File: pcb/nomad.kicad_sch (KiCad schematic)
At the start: 0 parts

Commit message: Fixing pcb project's .gitignore & initializing Kicad project
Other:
- title: (none) -> Nomad
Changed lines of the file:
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@@
 	(generator_version "10.0")
 	(paper "A4")
+	(title_block
+		(title "Nomad")
+		(rev "[In dev]")
+		(comment 1 "By @0Zane")
+		(comment 2 "Built for @Hackclub")
+	)
 	(sheet_instances
 		(path "/"

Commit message: Placing MCP9808 symbol
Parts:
- added R1, R2: 4.7k, symbol Device:R
- added U1: MCP9808_MSOP, Package_SO:MSOP-8_3x3mm_P0.65mm, symbol Sensor_Temperature:MCP9808_MSOP
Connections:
- new net: R1.2, U1.1 (SDA)
- new net: R2.2, U1.2 (SCL)
- new net +3V3: R1.1, R2.1, U1.8 (V_{DD})
- new net GND: U1.4 (GND)
- no-connect marks 0 -> 1

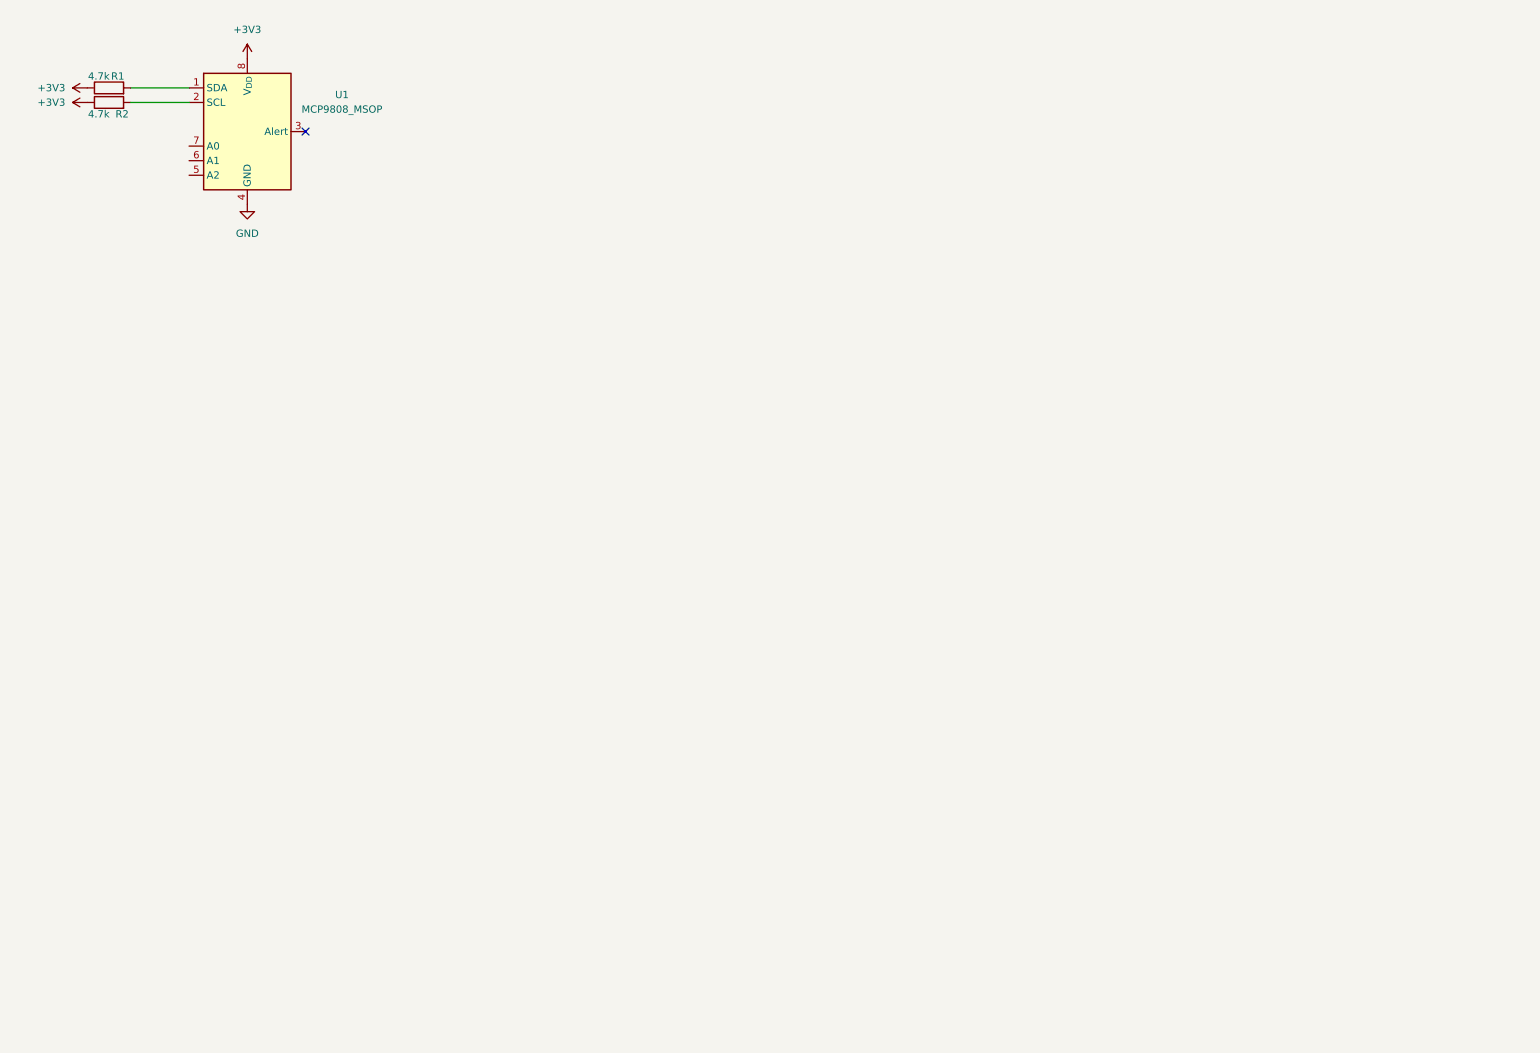
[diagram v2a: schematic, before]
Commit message: Wiring USB-C, MCP9808, PCF8574T
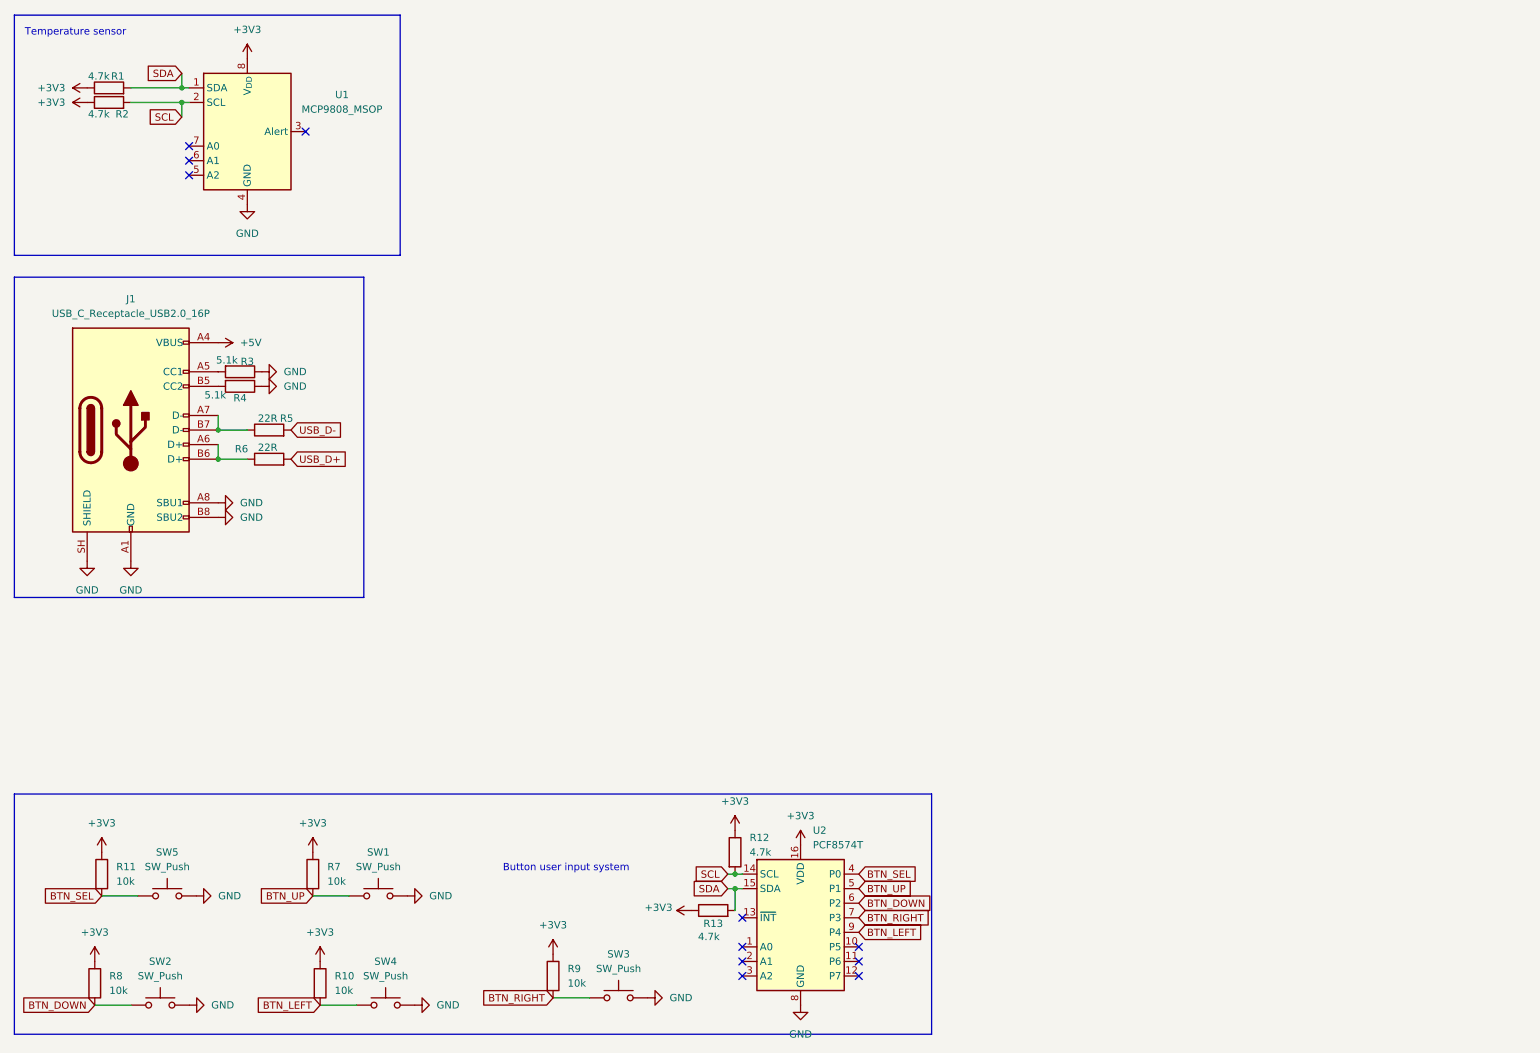
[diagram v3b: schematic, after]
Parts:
- added J1: USB_C_Receptacle_USB2.0_16P, symbol Connector:USB_C_Receptacle_USB2.0_16P
- added R10, R11, R7, R8, R9: 10k, symbol Device:R
- added R12, R13: 4.7k, symbol Device:R
- added R3, R4: 5.1k, symbol Device:R
- added R5, R6: 22R, symbol Device:R
- added SW1, SW2, SW3, SW4, SW5: SW_Push, symbol Switch:SW_Push
- added U2: PCF8574T, Package_SO:SOIC-16W_7.5x10.3mm_P1.27mm, symbol Interface_Expansion:PCF8574T
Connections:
- net +3V3: now also R10.1, R11.1, R12.1, R13.1, R7.1, R8.1, R9.1, U2.16 (VDD)
- net GND: now also J1.A1 (GND), J1.A12 (GND), J1.A8 (SBU1), J1.B1 (GND), J1.B12 (GND), J1.B8 (SBU2), J1.SH (SHIELD), R3.1, R4.1, SW1.2, SW2.2, SW3.2, SW4.2, SW5.2, U2.8 (GND)
- net SDA: now reaches R1.2, U1.1 (SDA)
- net SDA: now also R13.2, U2.15 (SDA)
- net SCL: now reaches R2.2, U1.2 (SCL)
- net SCL: now also R12.2, U2.14 (SCL)
- new net: J1.B5 (CC2), R4.2
- new net: J1.A6 (D+), J1.B6 (D+), R6.1
- new net: J1.A7 (D-), J1.B7 (D-), R5.1
- new net: J1.A5 (CC1), R3.2
- new net +5V: J1.A4 (VBUS), J1.A9 (VBUS), J1.B4 (VBUS), J1.B9 (VBUS)
- new net BTN_DOWN: R8.2, SW2.1, U2.6 (P2)
- new net BTN_LEFT: R10.2, SW4.1, U2.9 (P4)
- new net BTN_RIGHT: R9.2, SW3.1, U2.7 (P3)
- new net BTN_SEL: R11.2, SW5.1, U2.4 (P0)
- new net BTN_UP: R7.2, SW1.1, U2.5 (P1)
- new net USB_D+: R6.2
- new net USB_D-: R5.2
- no-connect marks 1 -> 11
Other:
- note added: "Button user input system"
- note added: "Temperature sensor"

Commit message: Replacing temperature sensor schematic + adding INT pin on PCF8574
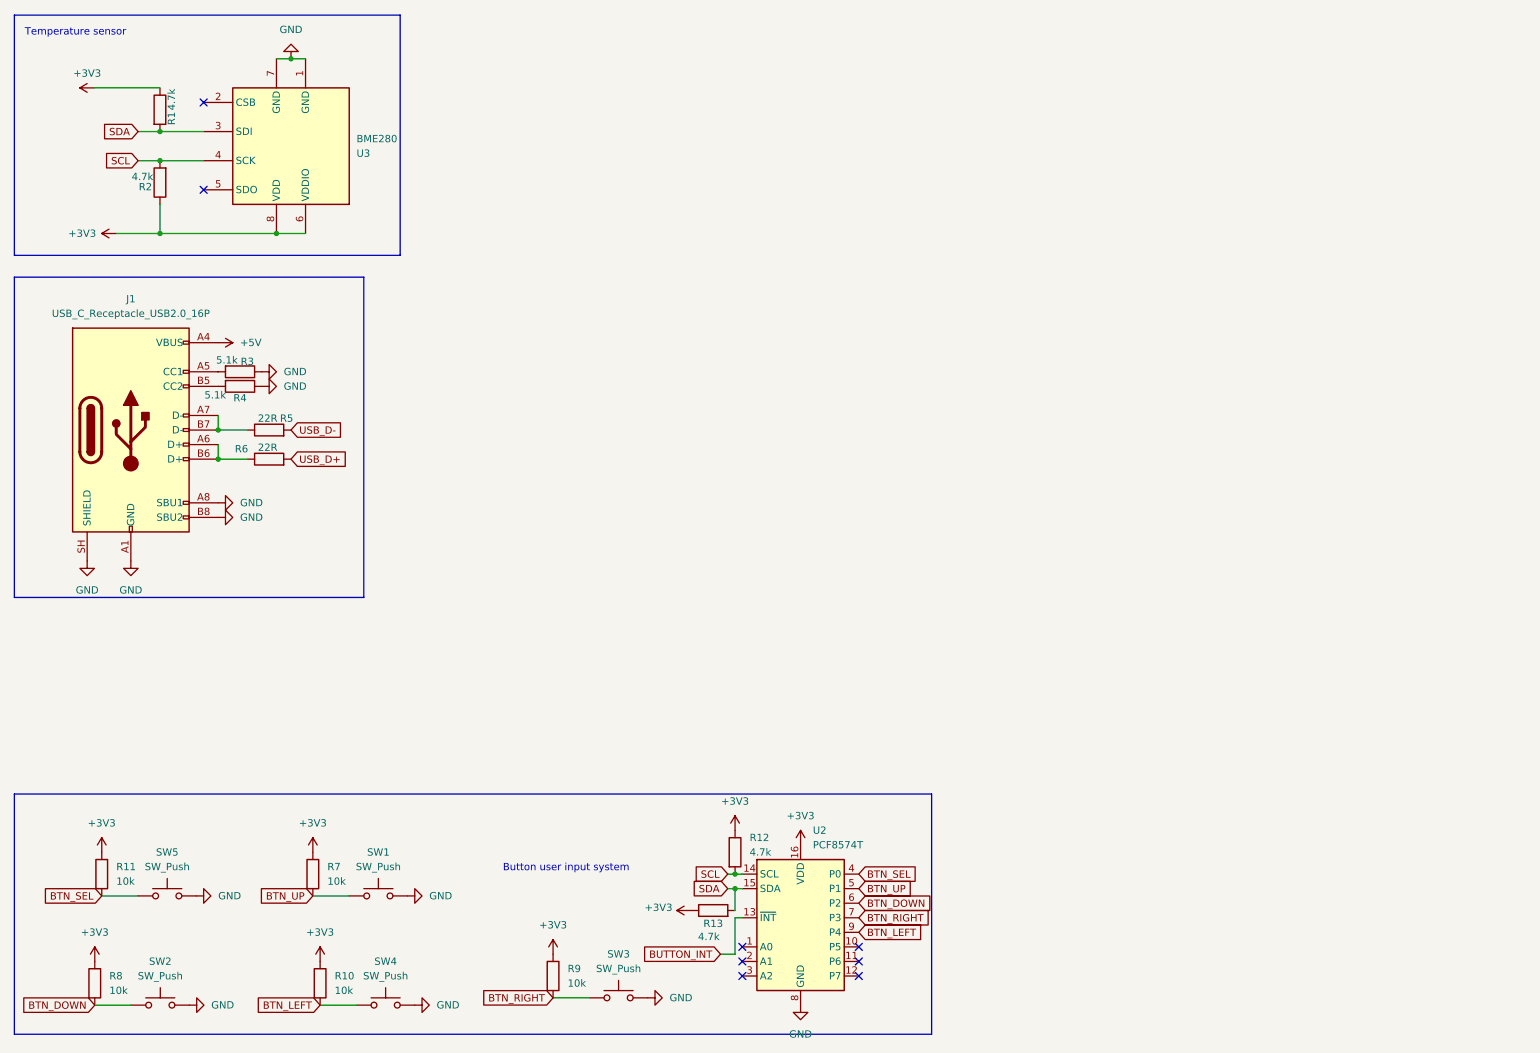
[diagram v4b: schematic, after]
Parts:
- removed U1: MCP9808_MSOP, Package_SO:MSOP-8_3x3mm_P0.65mm, symbol Sensor_Temperature:MCP9808_MSOP
- added U3: BME280, Package_LGA:Bosch_LGA-8_2.5x2.5mm_P0.65mm_ClockwisePinNumbering, symbol Sensor:BME280
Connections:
- net +3V3: now also U3.6 (VDDIO), U3.8 (VDD)
- net GND: now also U3.1 (GND), U3.7 (GND)
- net SCL: now also U3.4 (SCK)
- net SDA: now also U3.3 (SDI)
- net BUTTON_INT: now reaches U2.13 (~{INT})
- no-connect marks 11 -> 8
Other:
- moved on the sheet: R1, R2

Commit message: Adding BOOT & RESET buttons + ESP32 symbol
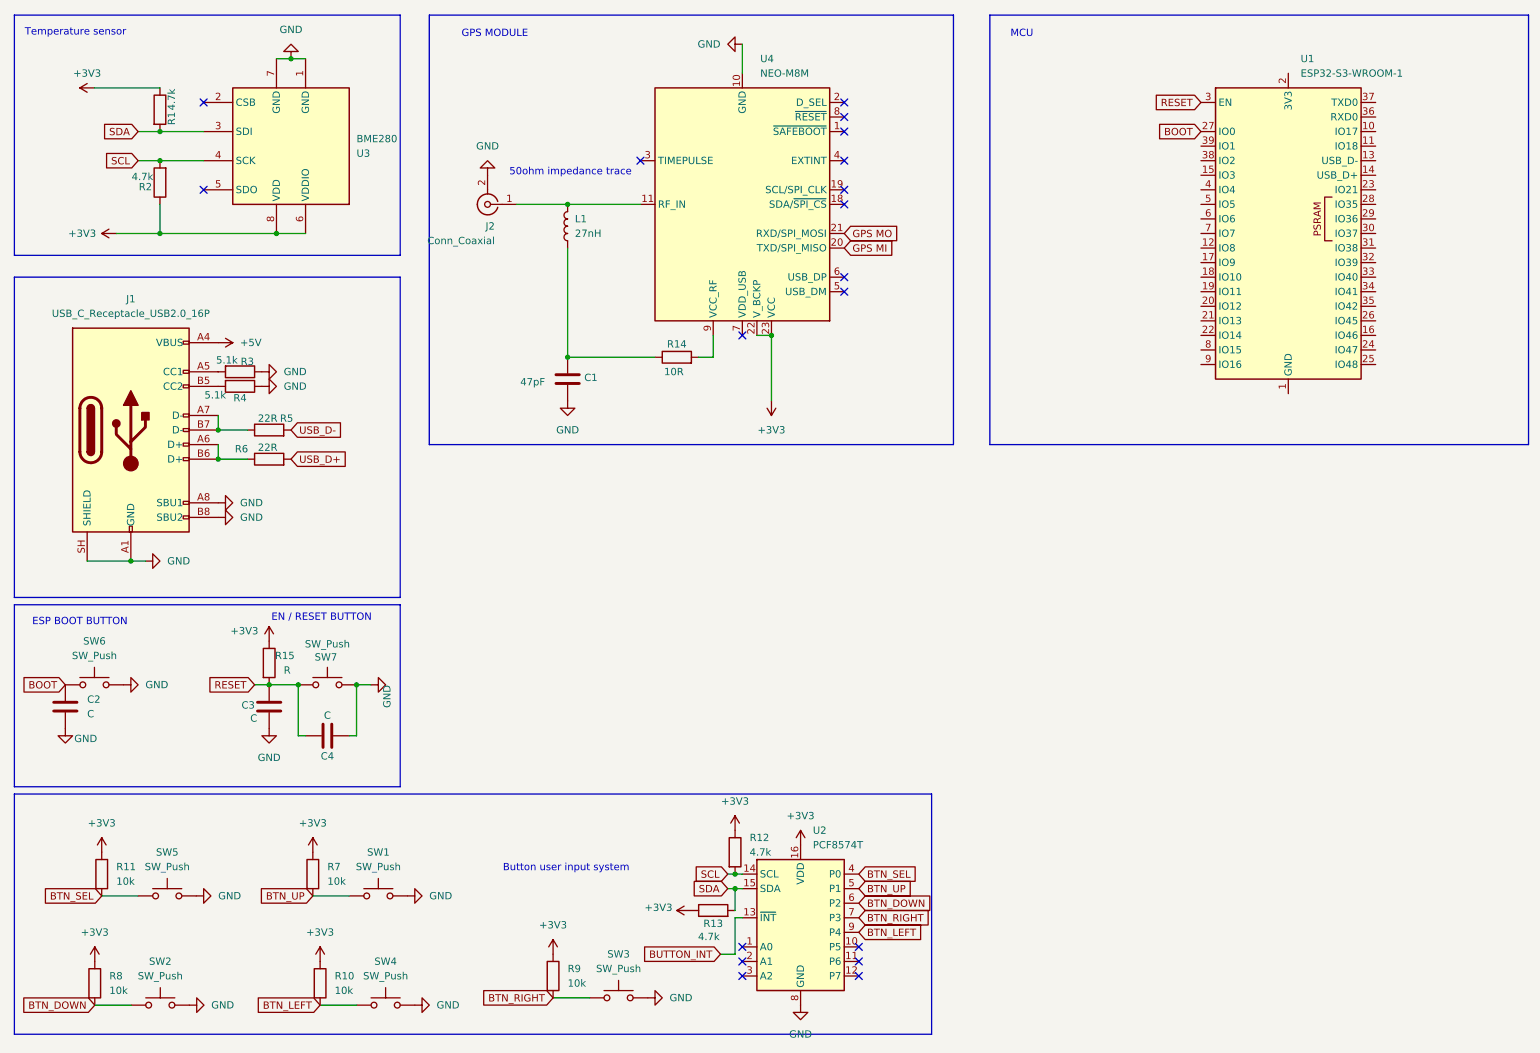
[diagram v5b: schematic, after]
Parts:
- added C1: 47pF, symbol Device:C
- added C2, C3, C4: C, symbol Device:C
- added J2: Conn_Coaxial, symbol Connector:Conn_Coaxial
- added L1: 27nH, symbol Device:L
- added R14: 10R, symbol Device:R
- added R15: R, symbol Device:R
- added SW6, SW7: SW_Push, symbol Switch:SW_Push
- added U1: ESP32-S3-WROOM-1, RF_Module:ESP32-S3-WROOM-1, symbol RF_Module:ESP32-S3-WROOM-1
- added U4: NEO-M8M, RF_GPS:ublox_NEO, symbol RF_GPS:NEO-M8M
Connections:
- net +3V3: now also R15.1, U4.22 (V_BCKP), U4.23 (VCC)
- net GND: now also C1.1, C2.2, C3.2, C4.2, J2.2 (Ext), SW6.2, SW7.2, U4.10 (GND), U4.12 (GND), U4.13 (GND), U4.24 (GND)
- new net: C1.2, L1.1, R14.1
- new net: R14.2, U4.9 (VCC_RF)
- new net: U1.1 (GND), U1.40 (GND), U1.41 (GND)
- new net: J2.1 (In), L1.2, U4.11 (RF_IN)
- new net BOOT: C2.1, SW6.1, U1.27 (IO0)
- new net GPS MI: U4.20 (TXD/SPI_MISO)
- new net GPS MO: U4.21 (RXD/SPI_MOSI)
- new net RESET: C3.1, C4.1, R15.2, SW7.1, U1.3 (EN)
- no-connect marks 8 -> 18
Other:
- note added: "50ohm impedance trace"
- note added: "EN / RESET BUTTON"
- note added: "ESP BOOT BUTTON"
- note added: "GPS MODULE"
- note added: "MCU"

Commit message: Adding voltage divider AMS1117 & USB to UART converter
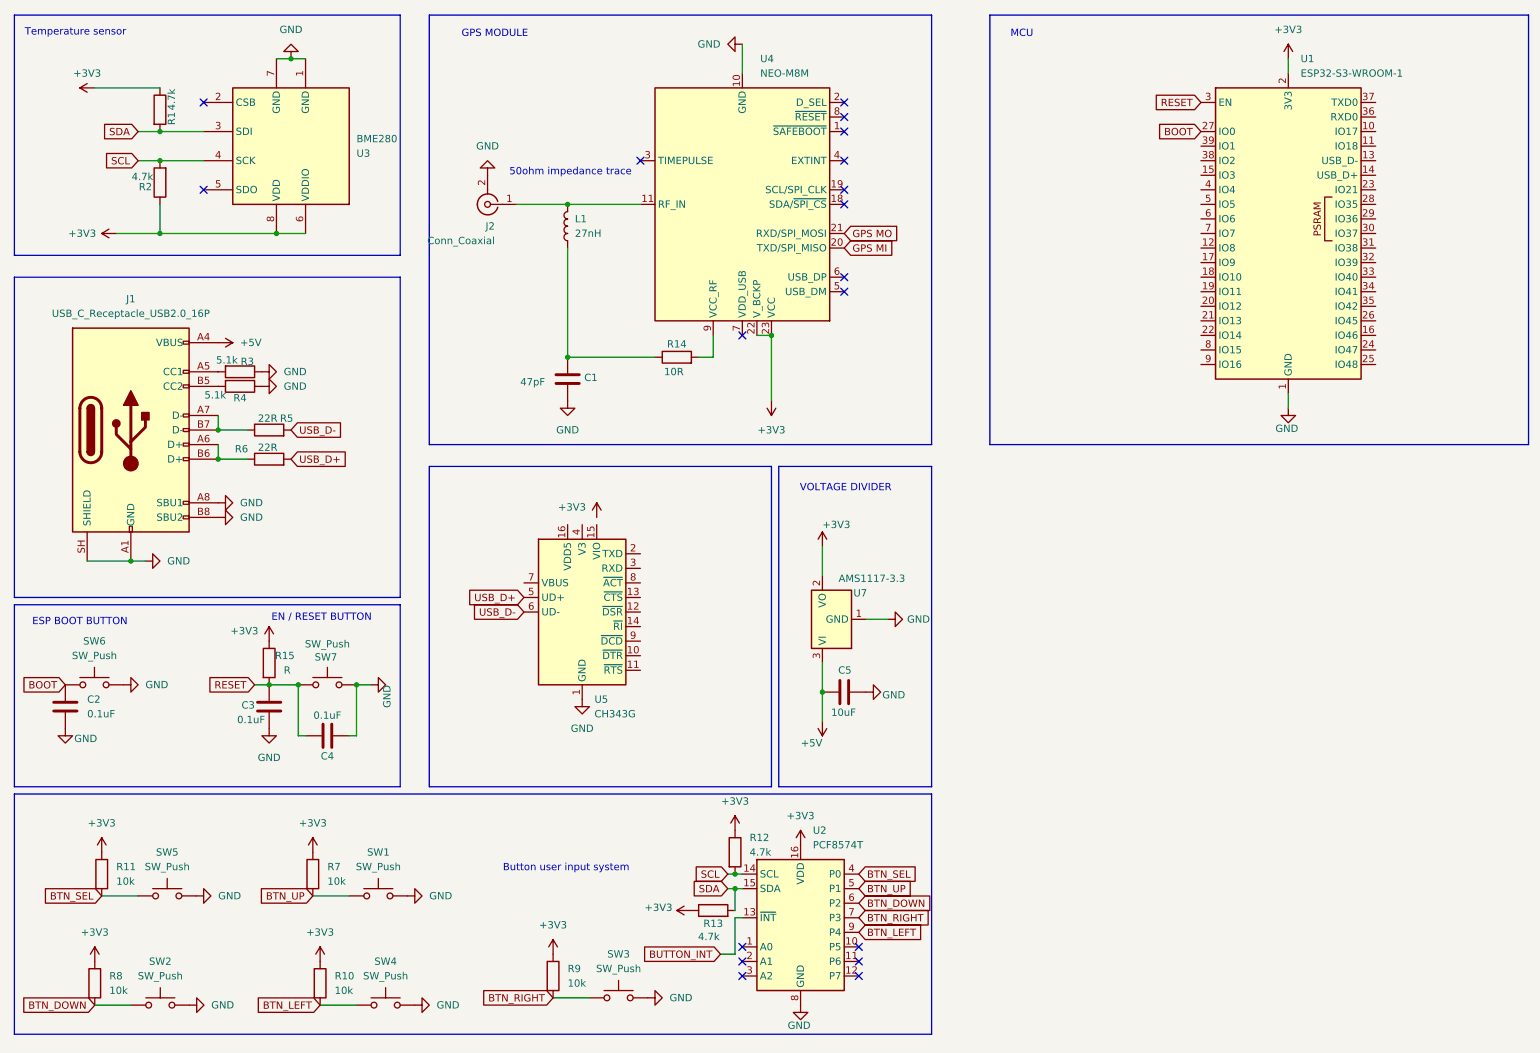
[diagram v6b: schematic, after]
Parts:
- added C5: 10uF, symbol Device:C
- added U5: CH343G, Package_SO:SOIC-16_3.9x9.9mm_P1.27mm, symbol Interface_USB:CH343G
- added U7: AMS1117-3.3, Package_TO_SOT_SMD:SOT-223-3_TabPin2, symbol Regulator_Linear:AMS1117-3.3
- C1: footprint (none) -> Capacitor_SMD:C_0805_2012Metric
- C2, C3, C4: value C -> 0.1uF; footprint (none) -> Capacitor_SMD:C_0805_2012Metric
- J1: footprint (none) -> Connector_USB:USB_C_Receptacle_HCTL_HC-TYPE-C-16P-01A
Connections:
- net +3V3: now also U1.2 (3V3), U7.2 (VO)
- net +5V: now also C5.1, U7.3 (VI)
- net GND: now also U1.1 (GND), U1.40 (GND), U1.41 (GND), C5.2, U5.1 (GND), U7.1 (GND)
- net USB_D+: now also U5.5 (UD+)
- net USB_D-: now also U5.6 (UD-)
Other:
- note added: "VOLTAGE DIVIDER"
